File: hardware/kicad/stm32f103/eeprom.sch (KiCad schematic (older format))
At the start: 2 parts, among them IC1 AT24CS02-SSHM

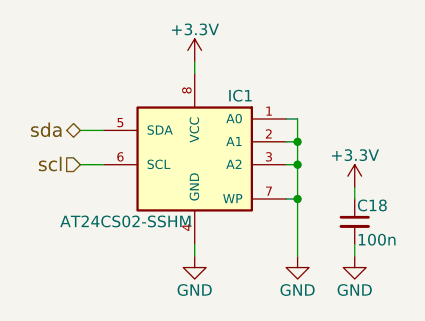
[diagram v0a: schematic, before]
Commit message: hardware/kicad/stm32f103: MCU/LED block ready
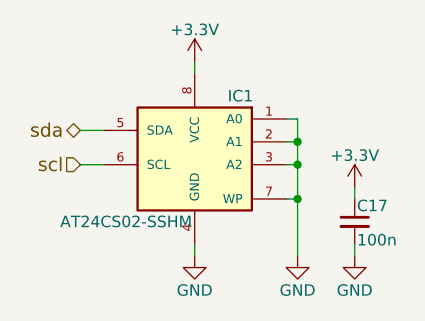
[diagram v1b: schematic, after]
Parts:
- renumbered C18 to C17
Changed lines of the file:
@@
 LIBS:transformer
 LIBS:stm32
-LIBS:stm32f030-cache
+LIBS:stm32f103-cache
 EELAYER 25 0
 EELAYER END
 $Descr A4 11693 8268
 encoding utf-8
-Sheet 6 6
+Sheet 5 5
 Title ""
 Date ""
@@
 $EndComp
 $Comp
-L +3.3V #PWR055
+L +3.3V #PWR047
 U 1 1 589C205E
 P 5600 2850
-F 0 "#PWR055" H 5600 2700 50  0001 C CNN
+F 0 "#PWR047" H 5600 2700 50  0001 C CNN
 F 1 "+3.3V" H 5600 2990 50  0000 C CNN
 F 2 "" H 5600 2850 50  0000 C CNN
@@
 $EndComp
 $Comp
-L GND #PWR056
+L GND #PWR048
 U 1 1 589C2085
 P 5600 3700
-F 0 "#PWR056" H 5600 3450 50  0001 C CNN
+F 0 "#PWR048" H 5600 3450 50  0001 C CNN
 F 1 "GND" H 5600 3550 50  0000 C CNN
 F 2 "" H 5600 3700 50  0000 C CNN
@@
 	6050 3300 6000 3300
 $Comp
-L GND #PWR057
+L GND #PWR049
 U 1 1 589C239F
 P 6050 3700
-F 0 "#PWR057" H 6050 3450 50  0001 C CNN
+F 0 "#PWR049" H 6050 3450 50  0001 C CNN
 F 1 "GND" H 6050 3550 50  0000 C CNN
 F 2 "" H 6050 3700 50  0000 C CNN
@@
 	5600 2900 5600 2850
 $Comp
-L C_Small C18
+L C_Small C17
 U 1 1 589CB0CF
 P 6300 3550
-F 0 "C18" H 6310 3620 50  0000 L CNN
+F 0 "C17" H 6310 3620 50  0000 L CNN
 F 1 "100n" H 6310 3470 50  0000 L CNN
 F 2 "Capacitors_SMD:C_0805_HandSoldering" H 6300 3550 50  0001 C CNN
@@
 $EndComp
 $Comp
-L +3.3V #PWR058
+L +3.3V #PWR050
 U 1 1 589CB128
 P 6300 3400
-F 0 "#PWR058" H 6300 3250 50  0001 C CNN
+F 0 "#PWR050" H 6300 3250 50  0001 C CNN
 F 1 "+3.3V" H 6300 3540 50  0000 C CNN
 F 2 "" H 6300 3400 50  0000 C CNN
@@
 $EndComp
 $Comp
-L GND #PWR059
+L GND #PWR051
 U 1 1 589CB139
 P 6300 3700
-F 0 "#PWR059" H 6300 3450 50  0001 C CNN
+F 0 "#PWR051" H 6300 3450 50  0001 C CNN
 F 1 "GND" H 6300 3550 50  0000 C CNN
 F 2 "" H 6300 3700 50  0000 C CNN
